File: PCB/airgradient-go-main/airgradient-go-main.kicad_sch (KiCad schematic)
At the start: 203 parts, among them CN1 HCZZ0032-5, CN2 HCZZ0032-5, CN3 HCZZ0032-5, Q1 SIA445EDJ-T1-GE3, Q2 ZVN4106FTA_C508255, Q3 CSD83325L, Q4 SS8050-G, Q5 SI1308EDL, SW1 TS-1091C-A1B3-D2, SW2 TS-1091C-A1B3-D2, U1 W25N512GVEIG, U10 SGP41-D-R4, U11 PS1-CO-SMOKE-10k, U12 SHT4x, U13 SPL07-003, U14 LIS2DH12TR, U15 TMUX121NKGR_C22428404, U16 S12, U17 TCA6408ARGT, U18 TAU1113, U19 LM66200DRLR, U2 ZDSD512MLGEAG, U20 LP5036, U3 BQ27742YZFR-G1, U4 ESP32-C5-MINI-1, U5 BQ25628RYKR, U6 HYG-8503A, U7 TPL5010DDCR, U8 TPS63802DLAR, U9 TPS7A0228DQNR, Y1 32.768kHz CL6pF

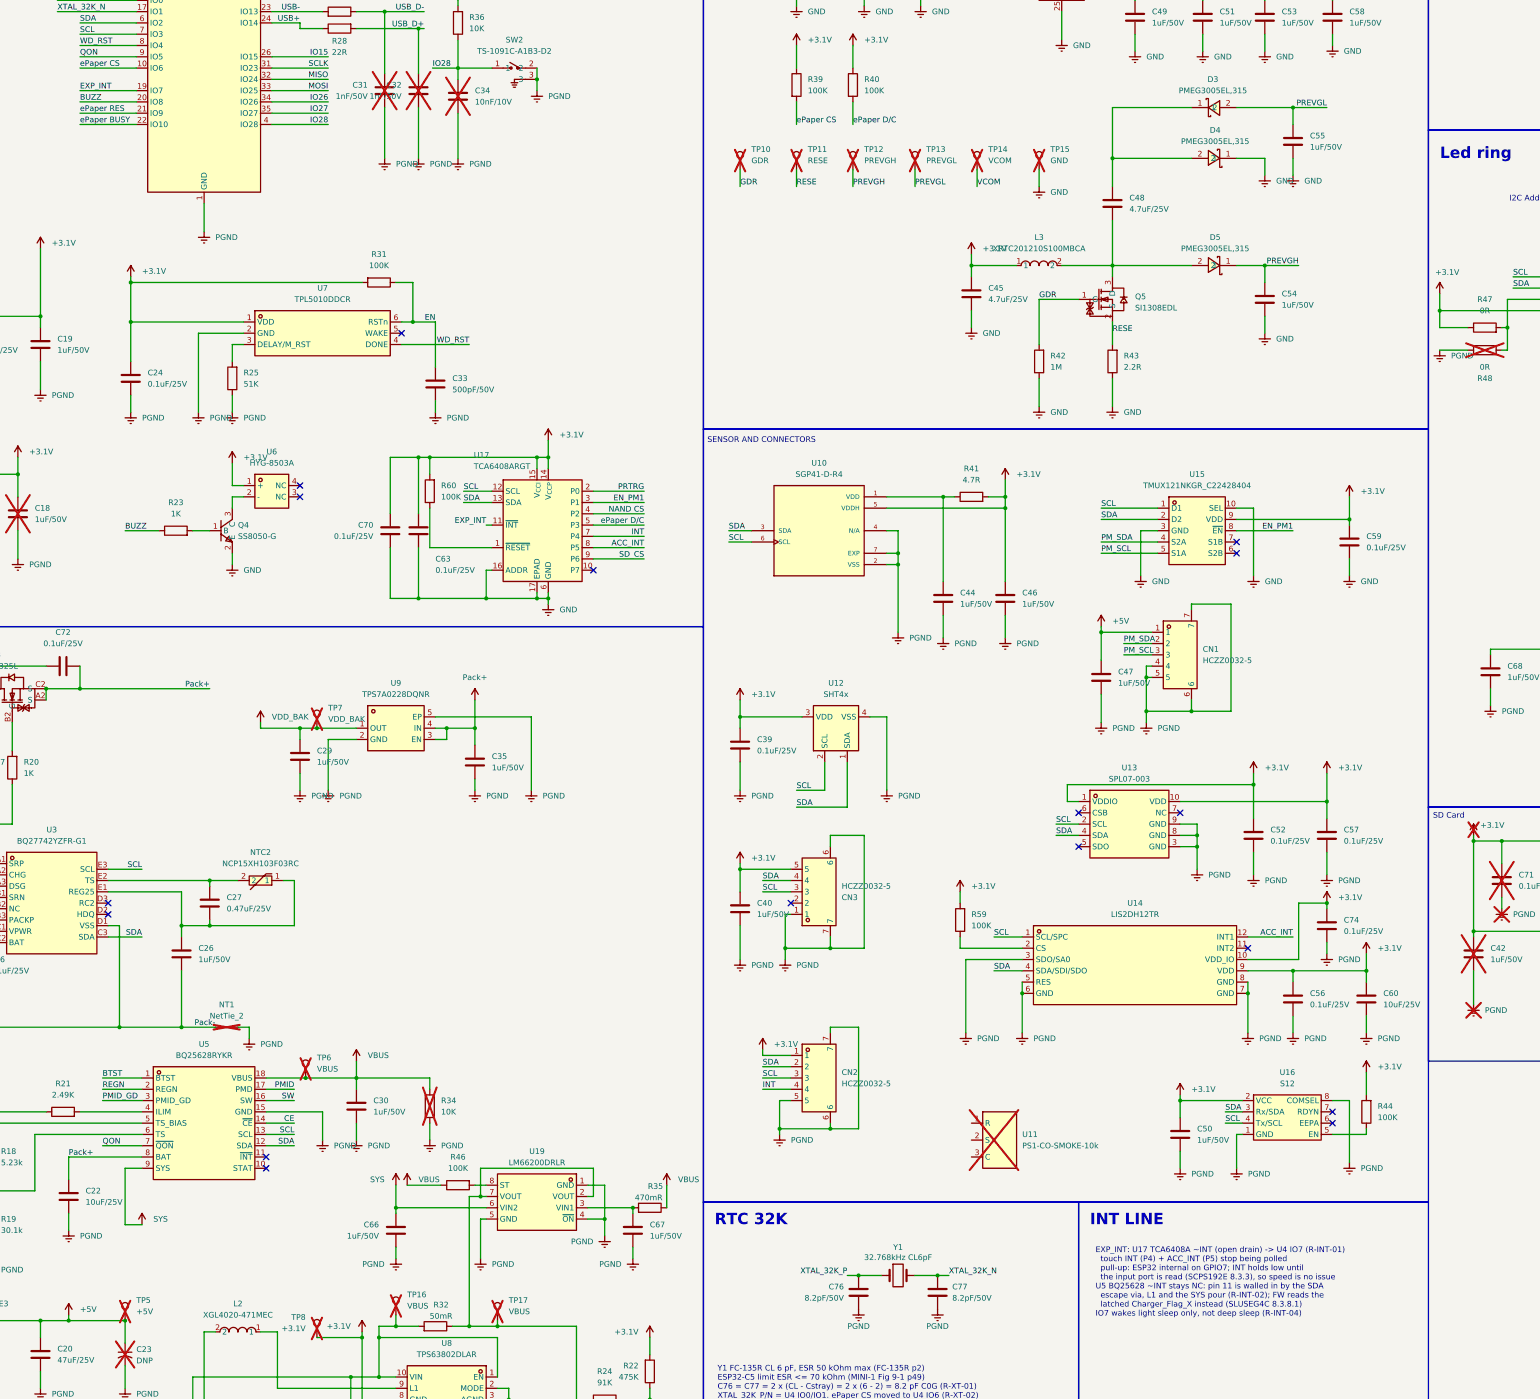
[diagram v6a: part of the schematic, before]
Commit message: Wire-OR the charger INT back onto IO7 (I2C_INT)
The layout now has an escape for U5 pin 11, so the charger INT joins
the expander INT again: U5 ~INT and U17 ~INT (both open drain) share
net I2C_INT into U4 IO7. U5 pin 11 loses its NC flag.

No external pull-up: GPIO7's internal pull-up (~45k) rises in about
1 us, far inside the charger's 256 us pulse, and the expander holds
its INT until read. Firmware reads the TCA6408A input port and the
latched Charger_Flag_X on every falling edge (R-INT-01..04).

lint: no new findings; ERC 269 -> 268 vs 1d977c7; net_diff 0 errors.
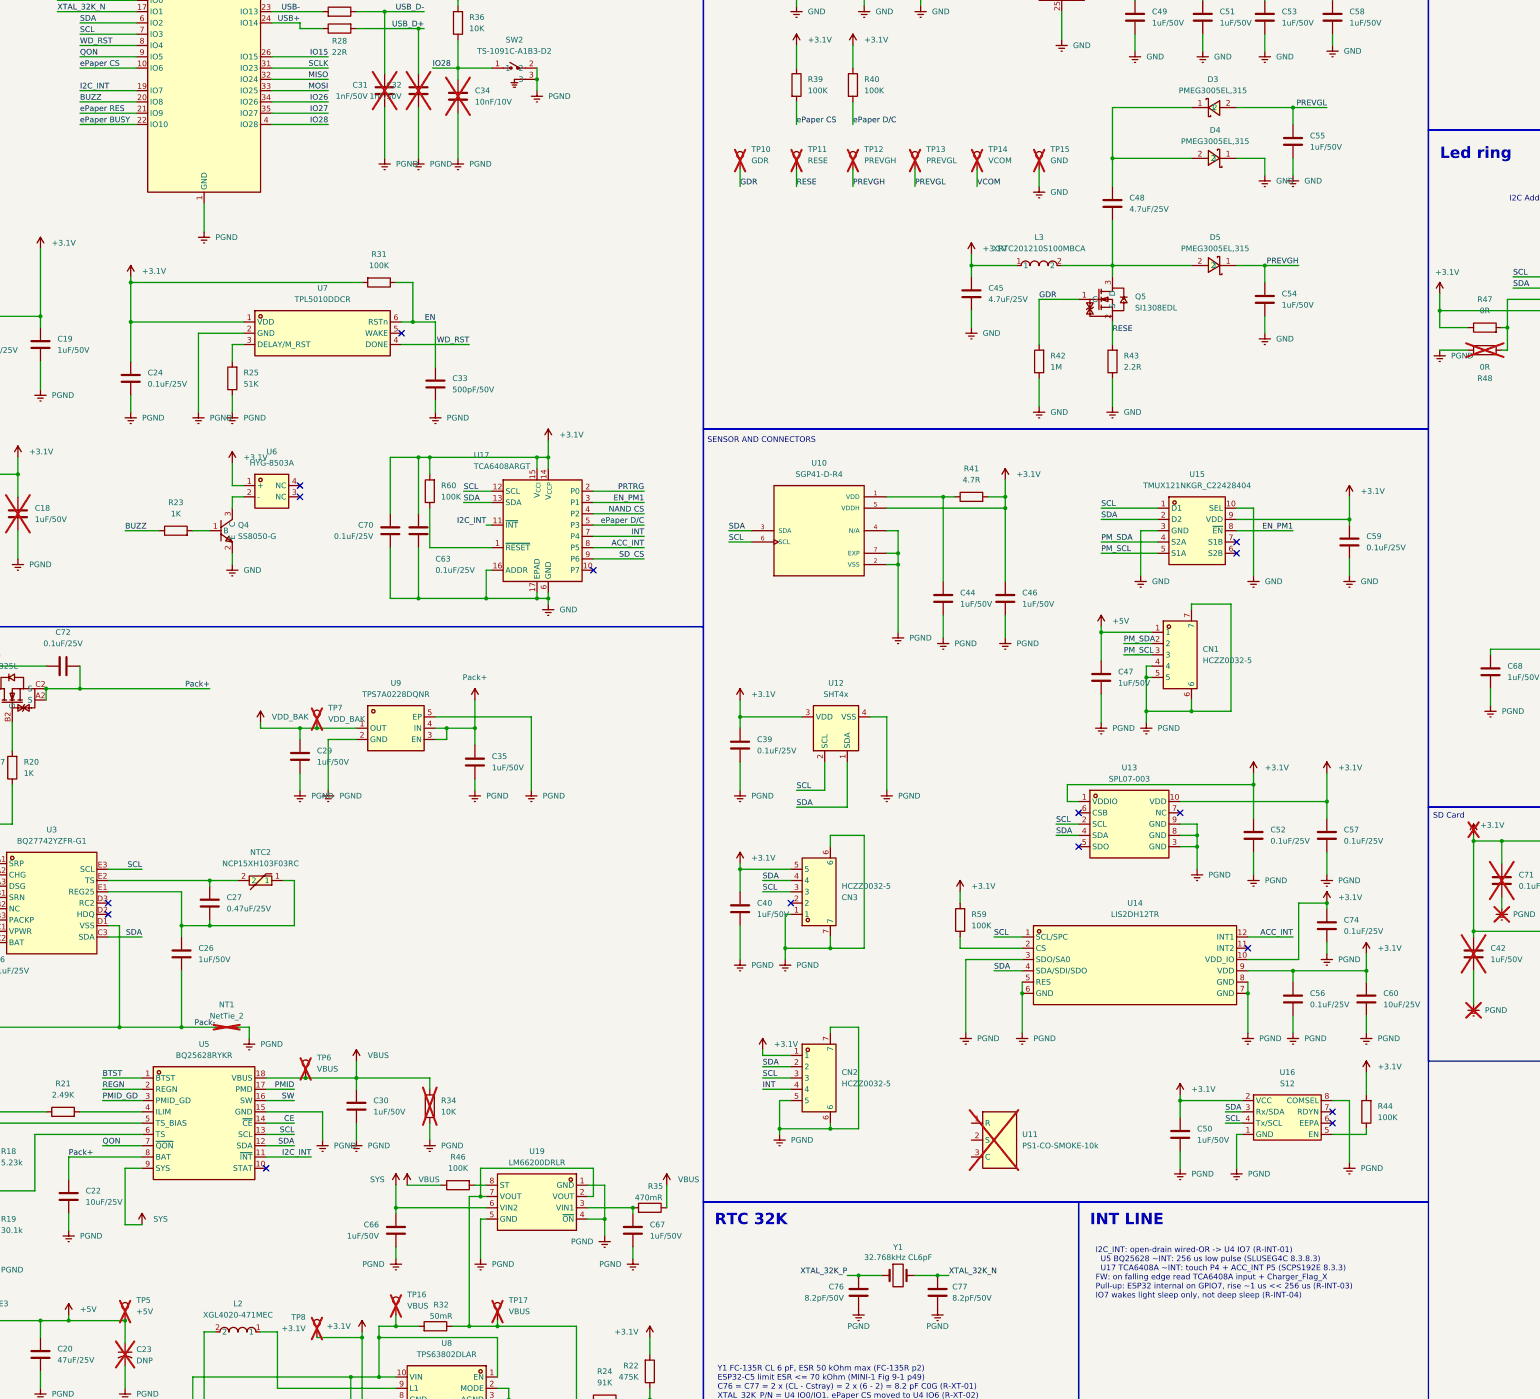
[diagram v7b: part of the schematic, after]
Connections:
- net EXP_INT is gone; now on net I2C_INT: U17.11 (~{INT}), U4.19 (IO7)
- net I2C_INT: now reaches U5.11 (~{INT})
- no-connect marks 30 -> 29
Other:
- note added: "I2C_INT: open-drain wired-OR -> U4 IO7 (R-INT-01) U5 BQ25628 ~INT: 256 us low pulse (SLUSEG4C 8.3.8.3) U17 TCA6408A ~INT: touch P4 + ACC_INT P5 (SCPS192E 8.3.3) FW: on falling edge read TCA6408A input + Charger_Flag_X Pull-up: ESP32 internal on GPIO7, rise ~1 us << 256 us (R-INT-03) IO7 wakes light sleep only, not deep sleep (R-INT-04)"
- note removed: "EXP_INT: U17 TCA6408A ~INT (open drain) -> U4 IO7 (R-INT-01) touch INT (P4) + ACC_INT (P5) stop being polled pull-up: ESP32 internal on GPIO7; INT holds low until the input port is read (SCPS192E 8.3.3), so speed is no issue U5 BQ25628 ~INT stays NC: pin 11 is walled in by the SDA escape via, L1 and the SYS pour (R-INT-02); FW reads the latched Charger_Flag_X instead (SLUSEG4C 8.3.8.1) IO7 wakes 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"
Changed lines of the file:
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@@
 	)
 	(no_connect
-		(at 162.56 323.85)
-	)
-	(no_connect
 		(at 162.56 326.39)
 	)
@@
 	(wire
 		(pts
+			(xy 162.56 323.85) (xy 172.72 323.85)
+		)
+		(stroke
+			(width 0)
+			(type default)
+		)
+	)
+	(label "I2C_INT"
+		(at 172.72 323.85 180)
+		(effects
+			(font
+				(size 1.27 1.27)
+			)
+			(justify right bottom)
+		)
+	)
+	(wire
+		(pts
 			(xy 213.36 181.61) (xy 212.09 181.61)
 		)
@@
 		)
 	)
-	(label "EXP_INT"
+	(label "I2C_INT"
 		(at 212.09 181.61 180)
 		(effects
@@
 		)
 	)
-	(label "EXP_INT"
+	(label "I2C_INT"
 		(at 120.65 83.82 0)
 		(effects
@@
 		)
 	)
-	(text "EXP_INT: U17 TCA6408A ~INT (open drain) -> U4 IO7 (R-INT-01)\n  touch INT (P4) + ACC_INT (P5) stop being polled\n  pull-up: ESP32 internal on GPIO7; INT holds low until\n  the input port is read (SCPS192E 8.3.3), so speed is no issue\nU5 BQ25628 ~INT stays NC: pin 11 is walled in by the SDA\n  escape via, L1 and the SYS pour (R-INT-02); FW reads the\n  latched Charger_Flag_X instead (SLUSEG4C 8.3.8.1)\nIO7 wakes light sleep only, not deep sleep (R-INT-04)"
+	(text "I2C_INT: open-drain wired-OR -> U4 IO7 (R-INT-01)\n  U5 BQ25628 ~INT: 256 us low pulse (SLUSEG4C 8.3.8.3)\n  U17 TCA6408A ~INT: touch P4 + ACC_INT P5 (SCPS192E 8.3.3)\nFW: on falling edge read TCA6408A input + Charger_Flag_X\nPull-up: ESP32 internal on GPIO7, rise ~1 us << 256 us (R-INT-03)\nIO7 wakes light sleep only, not deep sleep (R-INT-04)"
 		(exclude_from_sim no)
 		(at 349.25 344.17 0)

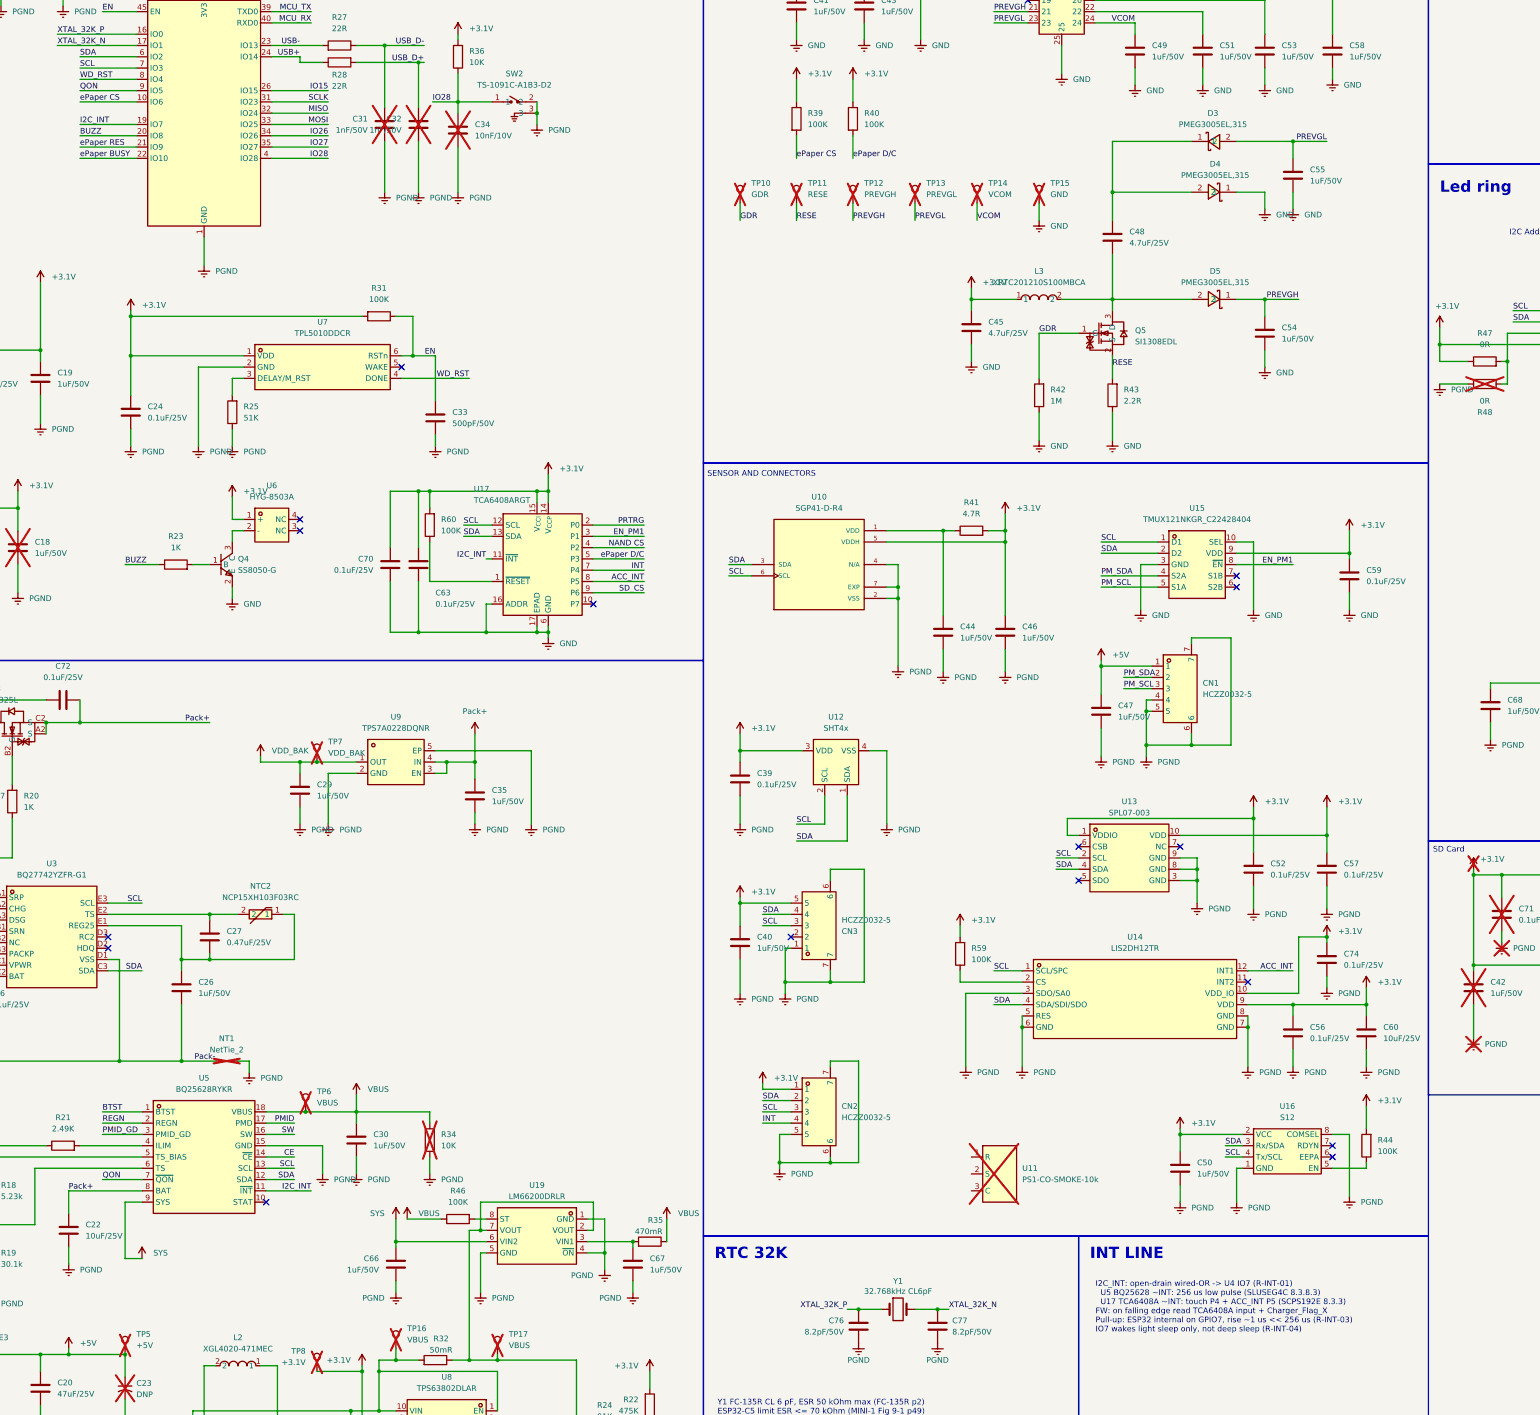
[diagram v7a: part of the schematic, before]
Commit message: Split the charger INT onto IO15 (CHG_INT)
The wired-OR on IO7 becomes two lines, so each edge names its source:
U5 ~INT -> CHG_INT -> U4 IO15 (pad 26), U17 ~INT -> EXP_INT -> U4 IO7
(pad 19). Both use the GPIO internal pull-up; neither wakes the chip
from deep sleep.

Layout: the charger route no longer joins the expander via. B.Cu turns
east under the module at y 55.48, passes under UART TX to one via at
(19.05,56.23), and F.Cu enters pad 26 from the west. The F.Cu/In2 tail
at y 61.9 and its 2 vias are gone: 65 mm / 6 vias instead of 68 / 7.

ERC 268 -> 267; DRC 230 = baseline, 0 unconnected, parity 0.
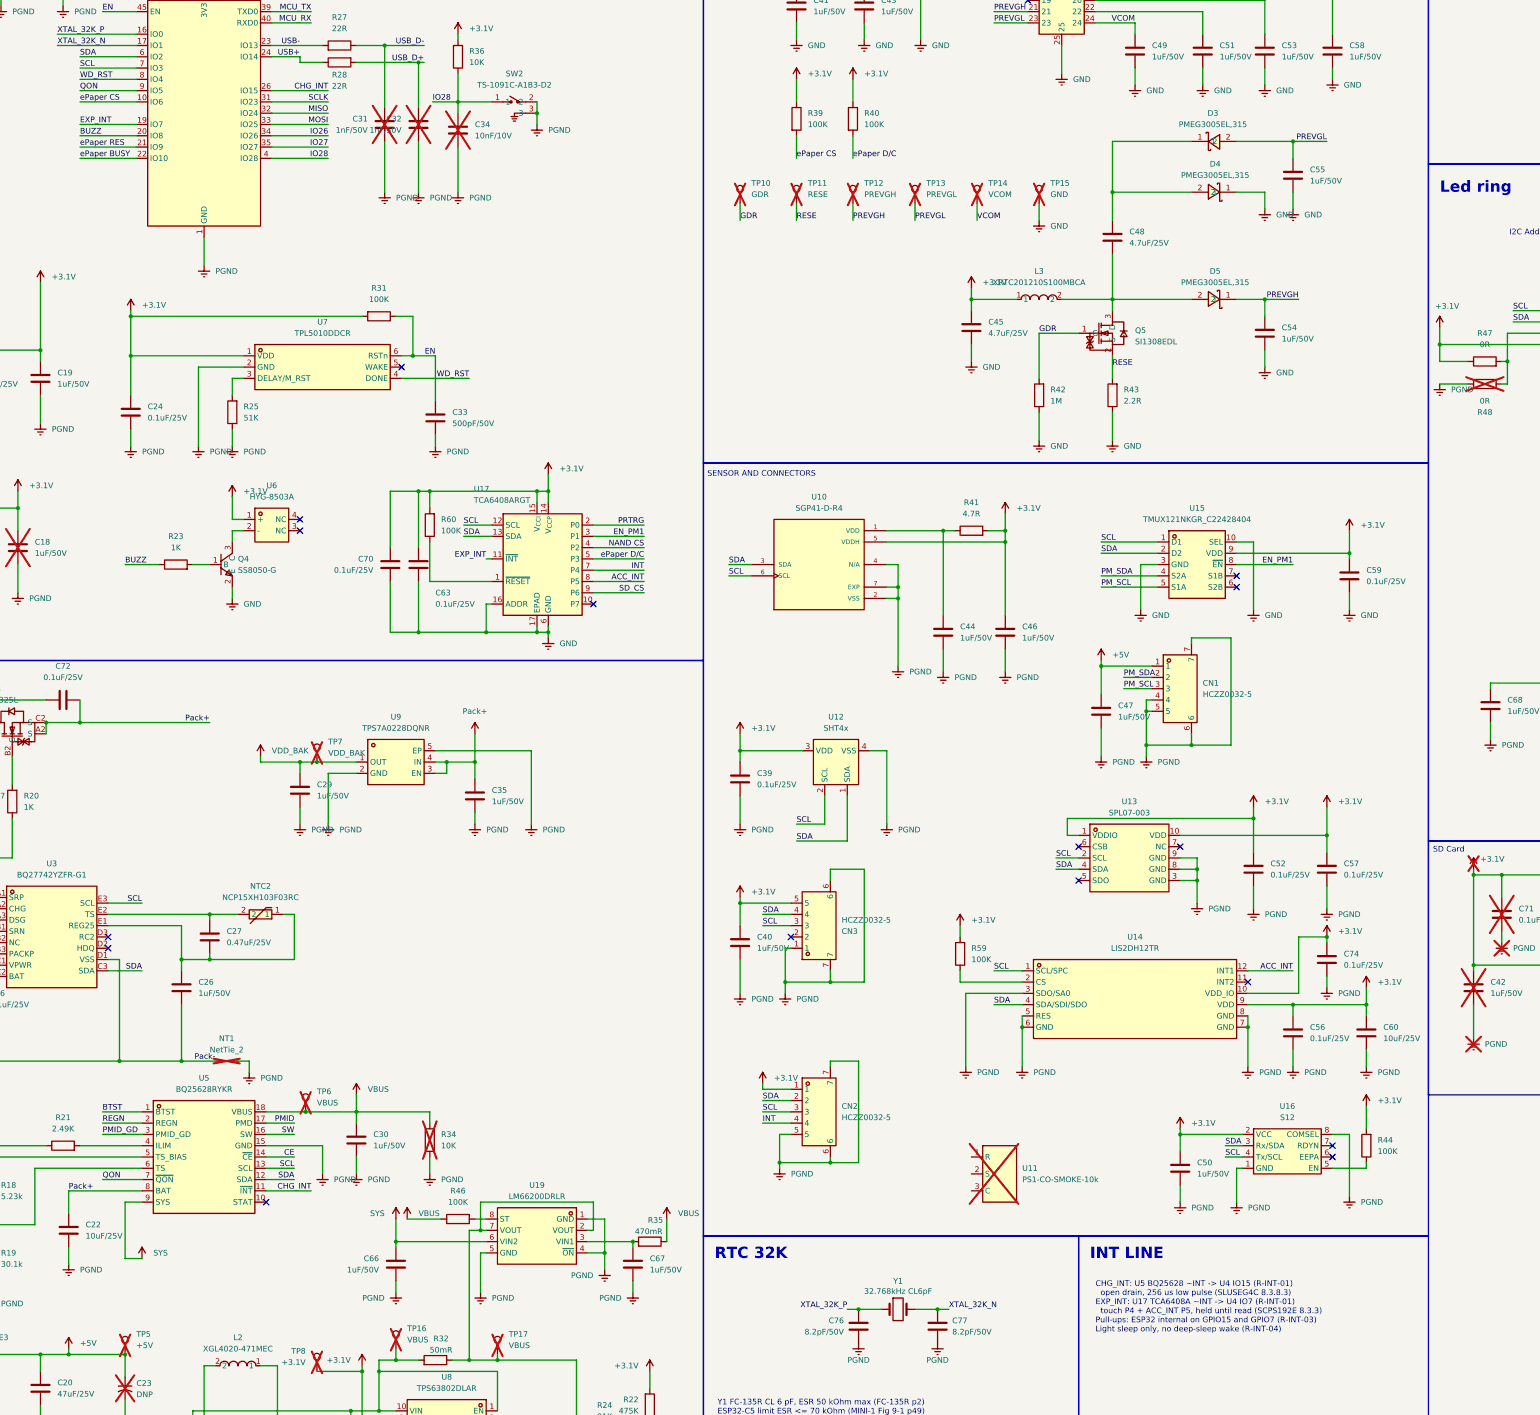
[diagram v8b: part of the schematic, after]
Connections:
- net I2C_INT renamed EXP_INT
- net EXP_INT: no longer U5.11 (~{INT})
- net IO15 renamed CHG_INT
- net CHG_INT: now also U5.11 (~{INT})
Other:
- note added: "CHG_INT: U5 BQ25628 ~INT -> U4 IO15 (R-INT-01) open drain, 256 us low pulse (SLUSEG4C 8.3.8.3) EXP_INT: U17 TCA6408A ~INT -> U4 IO7 (R-INT-01) touch P4 + ACC_INT P5, held until read (SCPS192E 8.3.3) Pull-ups: ESP32 internal on GPIO15 and GPIO7 (R-INT-03) Light sleep only, no deep-sleep wake (R-INT-04)"
- note removed: "I2C_INT: open-drain wired-OR -> U4 IO7 (R-INT-01) U5 BQ25628 ~INT: 256 us low pulse (SLUSEG4C 8.3.8.3) U17 TCA6408A ~INT: touch P4 + ACC_INT P5 (SCPS192E 8.3.3) FW: on falling edge read TCA6408A input + Charger_Flag_X Pull-up: ESP32 internal on GPIO7, rise ~1 us << 256 us (R-INT-03) IO7 wakes light sleep only, not deep sleep (R-INT-04)"
